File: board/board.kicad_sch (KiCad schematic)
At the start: 5 parts, among them J1 002_SPI_2x5, J3 007_ADC_2x5, J4 007_ADC_2x5, J5 007_ADC_2x5, J6 007_ADC_2x5

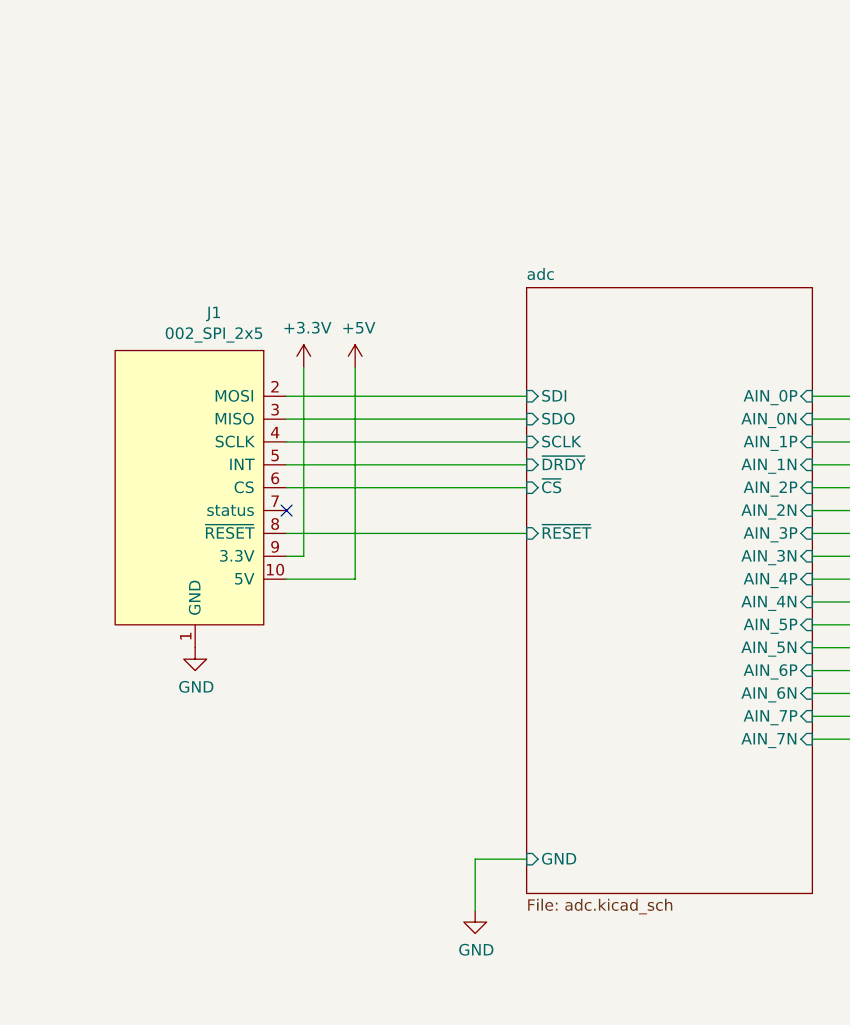
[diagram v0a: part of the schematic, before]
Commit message: separated gnd and agnd
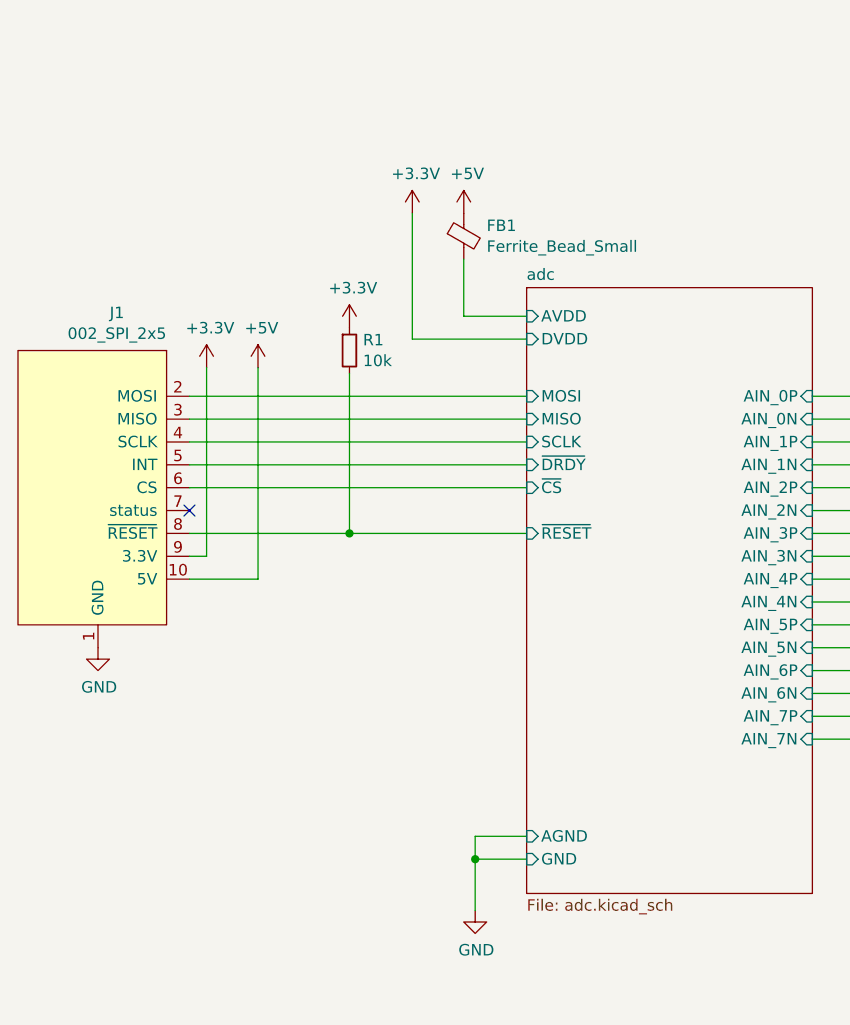
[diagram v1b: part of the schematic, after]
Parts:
- added FB1: Ferrite_Bead_Small, Inductor_SMD:L_0603_1608Metric, symbol Device:FerriteBead_Small
- added R1: 10k, Resistor_SMD:R_0603_1608Metric, symbol Device:R_Small
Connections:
- net +3.3V: now also R1.1
- net +5V: now also FB1.1
- net adc/~{RESET}: now also R1.2
- net adc/SDI renamed adc/MOSI
- net adc/SDO renamed adc/MISO
- new net adc/AVDD: FB1.2
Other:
- sheet adc ports: added AGND, AVDD, DVDD, MISO, MOSI; removed SDI, SDO
- moved on the sheet: J1
